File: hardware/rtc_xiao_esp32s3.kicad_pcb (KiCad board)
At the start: 4 copper layers, 17.5 x 21 mm, 25 parts, among them J1 +5V, J2 GND, J3 SCL, J4 SDA, J5 CLKOUT, J6 NINT, U1 RV-3028-C8

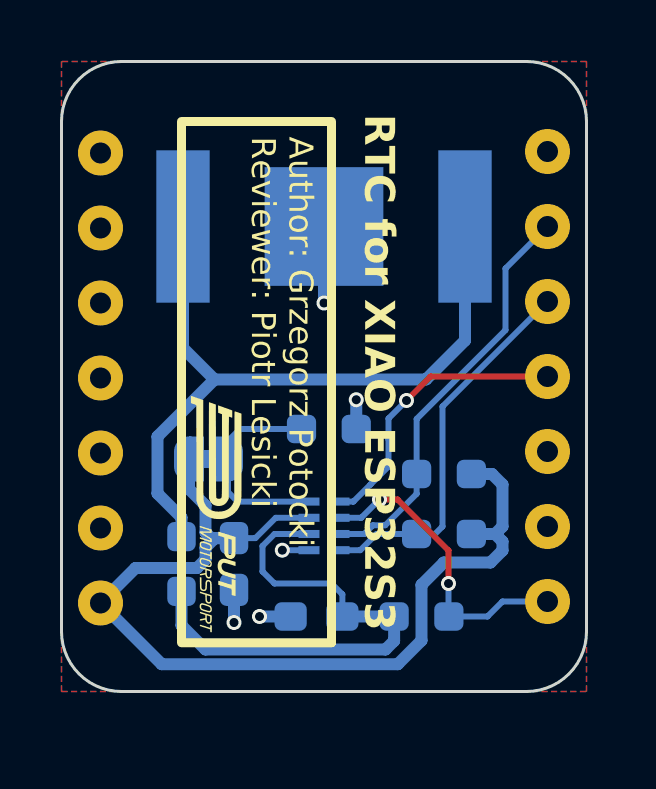
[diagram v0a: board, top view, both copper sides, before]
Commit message: nowe sockety 2.54mm
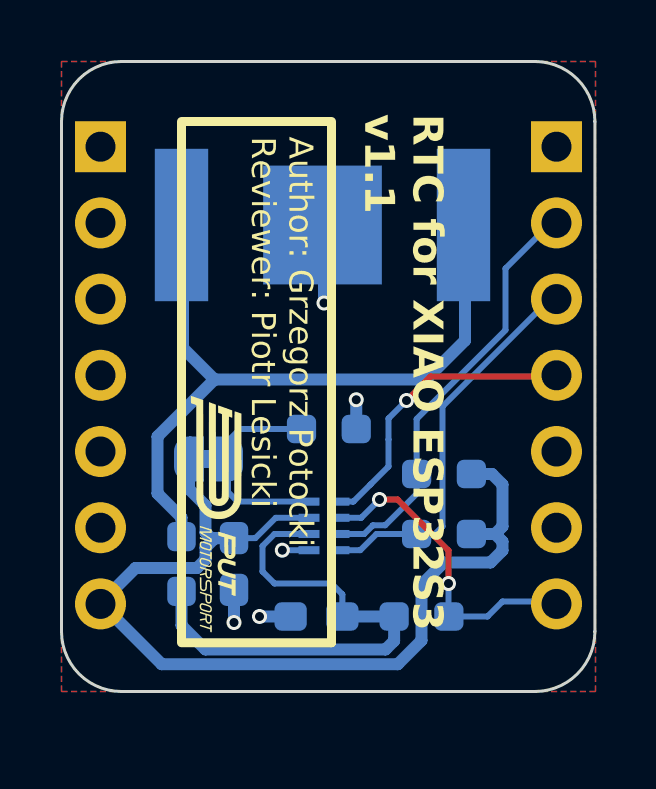
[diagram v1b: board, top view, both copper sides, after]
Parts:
- removed the J2 at (117.3, 98.0)
- removed the J2 at (132.2, 108.0)
- removed the J2 at (117.3, 100.5)
- removed the J2 at (117.3, 103.0)
- removed the J2 at (117.3, 110.5)
- removed the J2 at (132.2, 98.0)
- removed the J2 at (117.3, 105.5)
- removed the J2 at (132.2, 110.5)
- removed the J2 at (117.3, 108.0)
- removed J3: SCL, TestPoint:TestPoint_THTPad_D1.5mm_Drill0.7mm
- removed J4: SDA, TestPoint:TestPoint_THTPad_D1.5mm_Drill0.7mm
- removed J5: CLKOUT, TestPoint:TestPoint_THTPad_D1.5mm_Drill0.7mm
- removed J6: NINT, TestPoint:TestPoint_THTPad_D1.5mm_Drill0.7mm
- added J2: RIGHT, Connector_PinHeader_2.54mm:PinHeader_1x07_P2.54mm_Vertical, F.Cu at (132.5, 97.8)
- J1: value +5V -> LEFT; footprint TestPoint:TestPoint_THTPad_D1.5mm_Drill0.7mm -> Connector_PinHeader_2.54mm:PinHeader_1x07_P2.54mm_Vertical; moved to F.Cu
- moved J1 15.2 mm to (117.3, 97.8), turned to 0 degrees
- moved BT1 0.07 mm to (124.7, 100.5)
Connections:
- J1 pad 1: +5V -> GND
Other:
- board size 17.5 x 21 mm -> 17.8 x 21 mm
- board text added: "RTC for XIAO ESP32S3 v1.1"
- board text removed: "RTC for XIAO ESP32S3"

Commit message: update to kicad10 & pcb dimension adjusted, changed pinout - 5V removed, 3v3 added
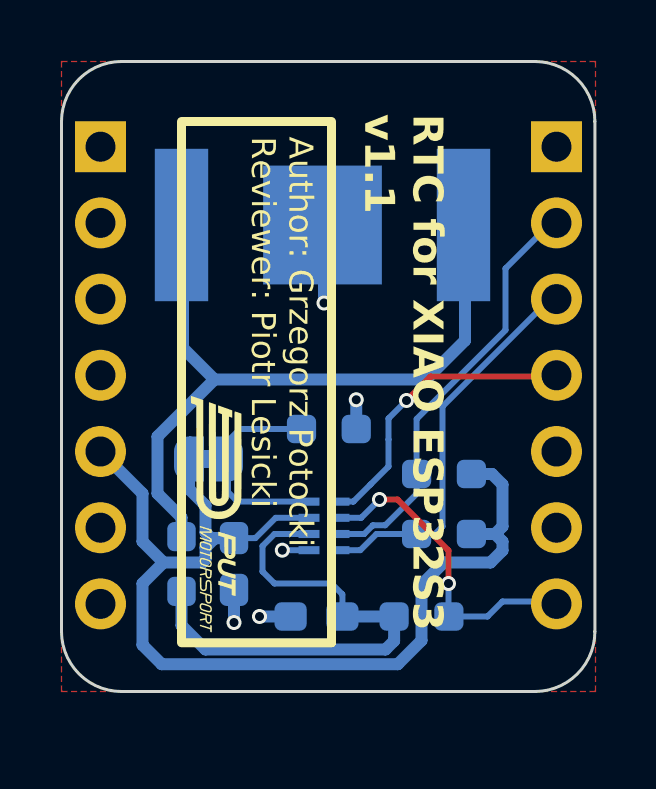
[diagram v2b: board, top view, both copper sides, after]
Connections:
- C1 pad 2: +5V -> +3V3
- J1 pad 1: GND -> unconnected-(J1-Pin_1-Pad1)
- J1 pad 2: GND -> unconnected-(J1-Pin_2-Pad2)
- J1 pad 3: GND -> unconnected-(J1-Pin_3-Pad3)
- J1 pad 4: GND -> unconnected-(J1-Pin_4-Pad4)
- J1 pad 5: GND -> +3V3
- J1 pad 7: +5V -> unconnected-(J1-Pin_7-Pad7)
- J2 pad 1: GND -> unconnected-(J2-Pin_1-Pad1)
- J2 pad 5: GND -> unconnected-(J2-Pin_5-Pad5)
- J2 pad 6: GND -> unconnected-(J2-Pin_6-Pad6)
- JP1 pad 2: +5V -> +3V3
- R2 pad 1: +5V -> +3V3
- R3 pad 1: +5V -> +3V3
- U1 pad 7: +5V -> +3V3
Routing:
- net +3V3: track 0.00 -> 36.3 mm
- net +5V: track 33.3 -> 0.00 mm
- removed copper zone on B.Cu, net GND
